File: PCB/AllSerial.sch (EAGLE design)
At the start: 99 parts, among them IC10 FT232RL, IC11 NCP1117ST33, IC20 MAX485CSA, IC3 74HCT02D, IC31 MAX489CSD, IC4 MAX485CSA, IC5 MAX211ECWI, IC6 MCP2003, IC7 MAX14932, IC8 MAX14932, IC9 MAX14932, J1 MA03-1W, Q1 IRF7416, Q2 BC857C, Q3 BC857C, Q4 BC857C, Q5 BC857C, Q6 BC857C, T4 BC847, X1 AKL18X-10W, X10 ALLSERIALD, X11 ALLSERIALD, X12 ALLSERIALD, X14 ALLSERIALMM, X2 MINI-USB-32005-201, X3 AKL18X-04W, X5 AKL18X-10W, X6 AKL18X-03W, X7 AKL18X-04W, X8 ALLSERIALD, X9 ALLSERIALD

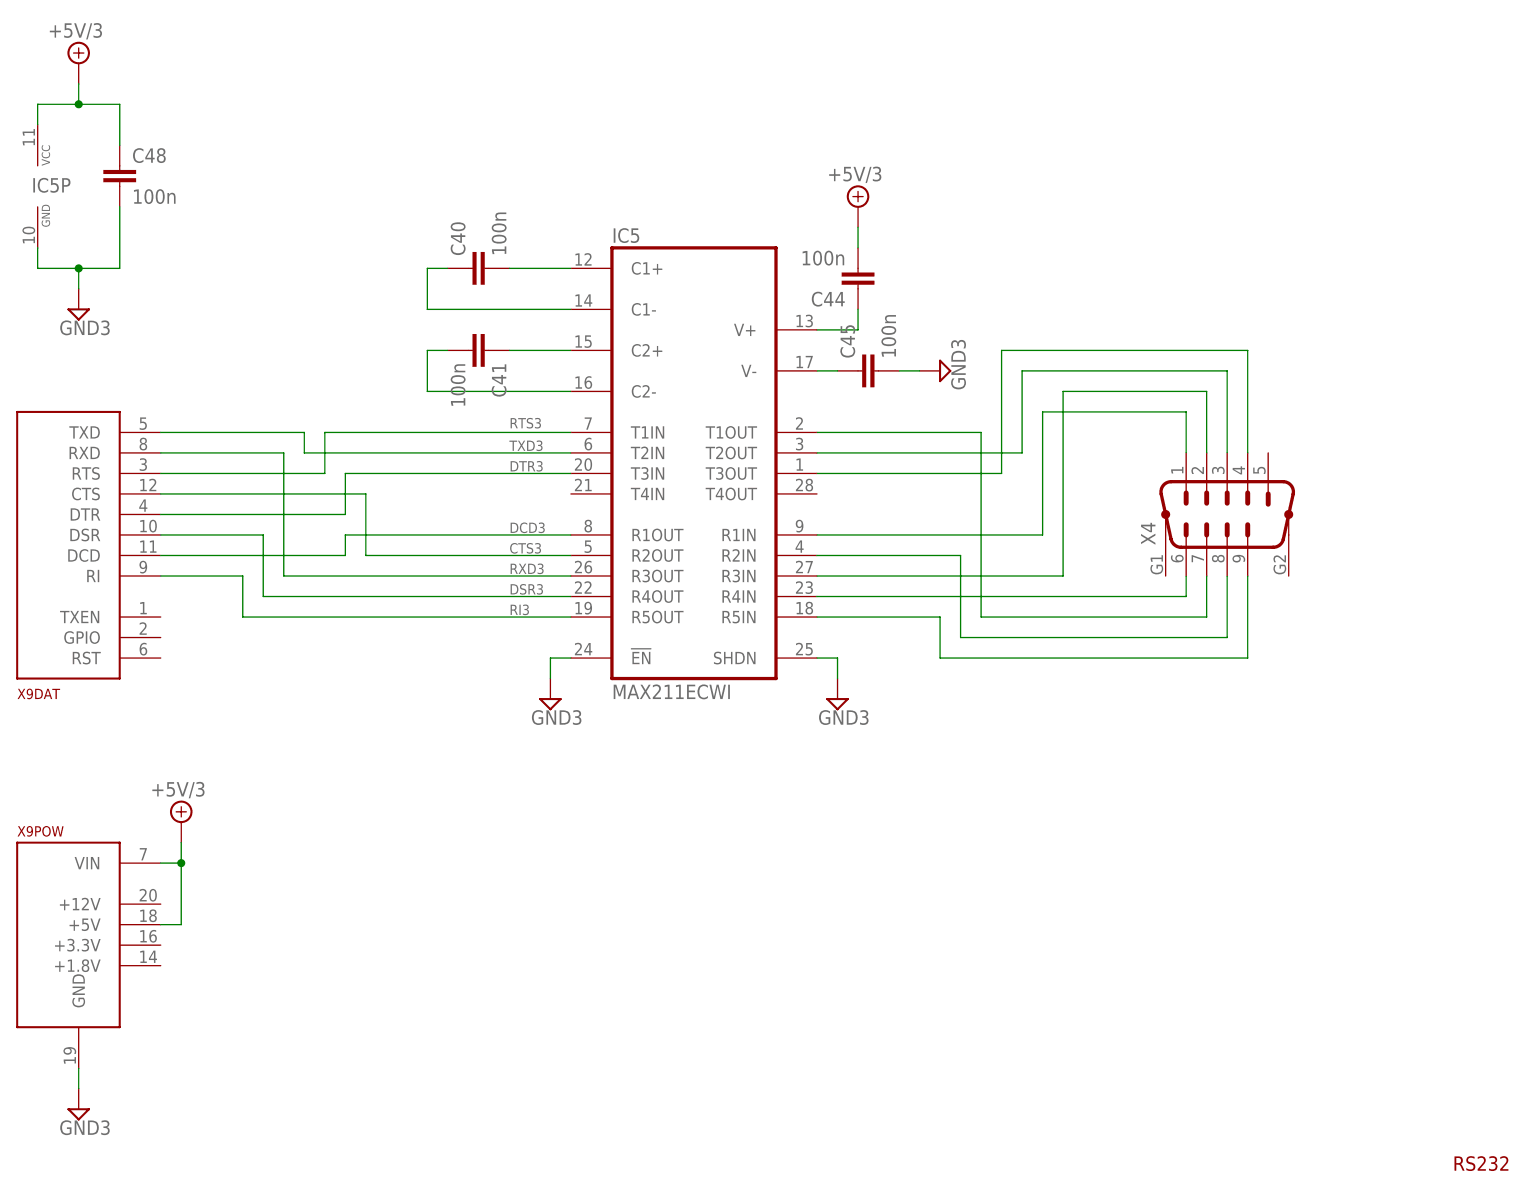
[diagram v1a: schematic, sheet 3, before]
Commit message: RS232 routing
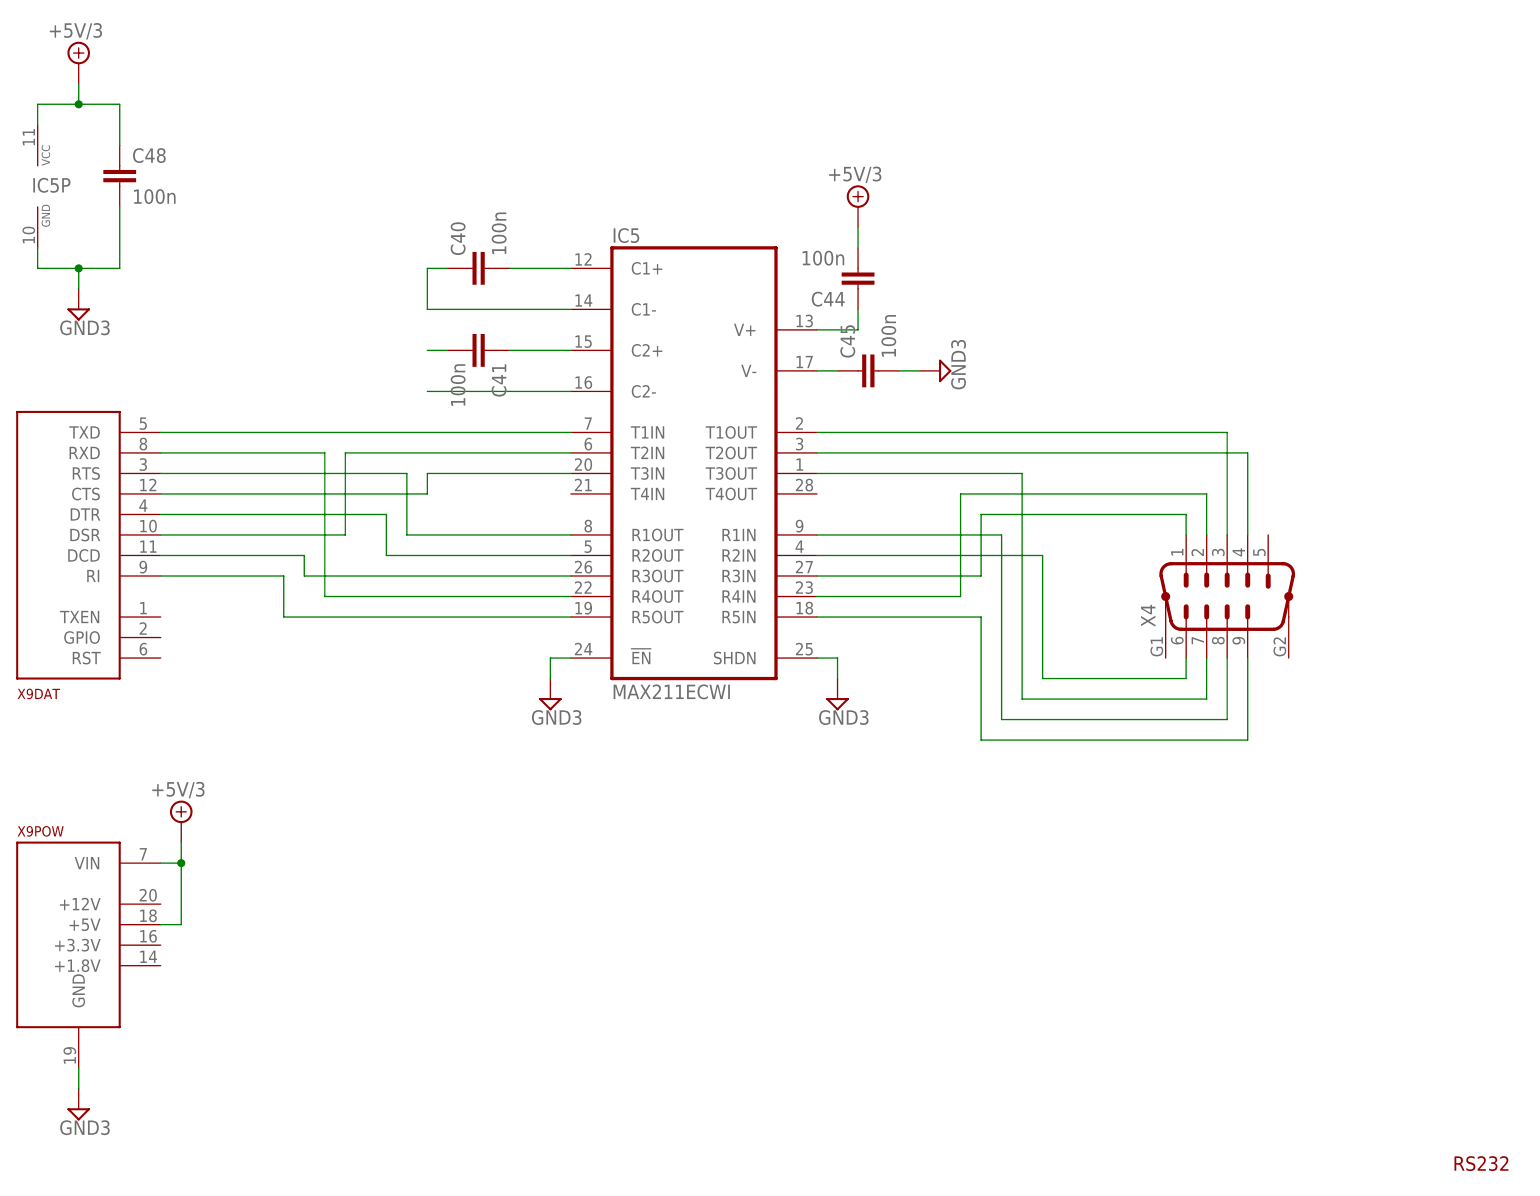
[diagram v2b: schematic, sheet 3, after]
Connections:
- net RI3 renamed N$98
- removed net CTS3: IC5G$1.R2OUT, X9DAT.CTS
- removed net DCD3: IC5G$1.R1OUT, X9DAT.DCD
- removed net DSR3: IC5G$1.R4OUT, X9DAT.DSR
- removed net DTR3: IC5G$1.T3IN, X9DAT.DTR
- removed net N$9 (its old number): IC5G$1.R1IN, X4.1
- removed net RTS3: IC5G$1.T1IN, X9DAT.RTS
- removed net RXD3: IC5G$1.R3OUT, X9DAT.RXD
- removed net TXD3: IC5G$1.T2IN, X9DAT.TXD
- new net N$100: IC5G$1.T2IN, X9DAT.DSR
- new net N$24: IC5G$1.T2OUT, X4.4
- new net N$92: C41.2
- new net N$93: IC5G$1.T1IN, X9DAT.TXD
- new net N$94: IC5G$1.R4OUT, X9DAT.RXD
- new net N$95: IC5G$1.T3IN, X9DAT.CTS
- new net N$96: IC5G$1.R1OUT, X9DAT.RTS
- new net N$97: IC5G$1.R3OUT, X9DAT.DCD
- new net N$99: IC5G$1.R2OUT, X9DAT.DTR
- net N$12: now also IC5G$1.R1IN, X4.8; no longer IC5G$1.R3IN, X4.2
- net N$15: now also IC5G$1.T3OUT, X4.7; no longer IC5G$1.T2OUT, X4.3
- net N$16: now also IC5G$1.R2IN, X4.6; no longer IC5G$1.T3OUT, X4.4
- net N$17: now also IC5G$1.R3IN, X4.1; no longer IC5G$1.R4IN, X4.6
- net N$18: now also IC5G$1.R4IN, X4.2; no longer IC5G$1.T1OUT, X4.7
- net N$23: now also IC5G$1.T1OUT, X4.3; no longer IC5G$1.R2IN, X4.8
- net N$28: no longer C41.2
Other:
- moved on the sheet: X4
